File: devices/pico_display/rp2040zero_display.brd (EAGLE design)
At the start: 38.2 x 20.6 mm, 13 parts, among them U1 RP2040-ZERO'

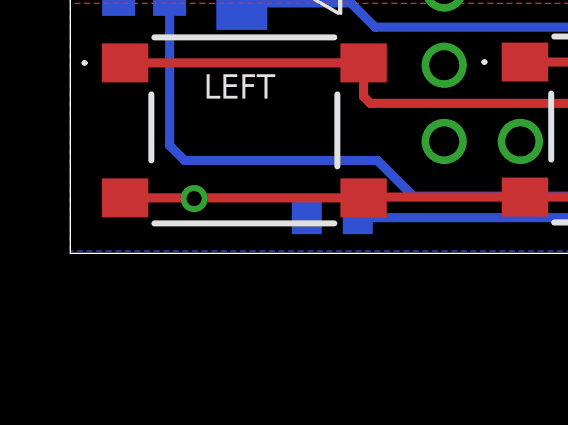
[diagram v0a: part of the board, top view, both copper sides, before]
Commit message: updates to beeper - now on main fdd board, updates to panel connectors
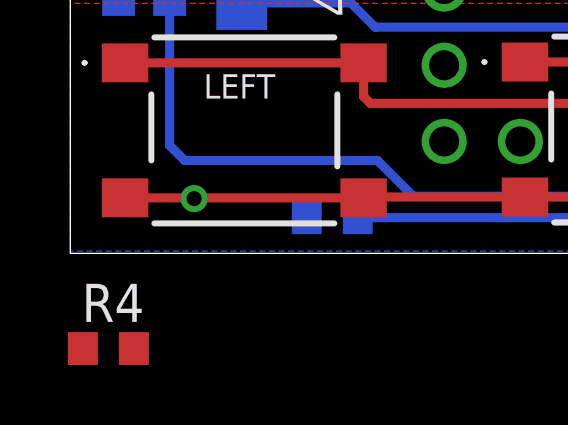
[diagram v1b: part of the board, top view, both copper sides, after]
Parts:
- added R4: 10k, resistor:R0603
- R1, R2: value 220R -> 1k
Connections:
- net RX_PANEL: now also R4.1
- net VCC: now also R4.2
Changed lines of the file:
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@@
 <attribute name="VALUE" x="10.38225" y="13.573125" size="1.27" layer="27" ratio="10" rot="R270"/>
 </element>
-<element name="R1" library="resistor" package="R0603" value="220R" x="6.429375" y="18.7325" smashed="yes" rot="MR90"/>
-<element name="R2" library="resistor" package="R0603" value="220R" x="6.429375" y="15.160625" smashed="yes" rot="MR270"/>
+<element name="R1" library="resistor" package="R0603" value="1k" x="6.429375" y="18.7325" smashed="yes" rot="MR90"/>
+<element name="R2" library="resistor" package="R0603" value="1k" x="6.429375" y="15.160625" smashed="yes" rot="MR270"/>
 <element name="D1" library="diode" package="DO214AC" value="SK110-DIO" x="5.715" y="10.398125" smashed="yes" rot="MR90"/>
 <element name="R3" library="resistor" package="R0603" value="0R" x="8.73125" y="1.190625" smashed="yes" rot="MR180"/>
@@
 <element name="R5" library="resistor" package="R0603" value="2k2" x="3.81" y="15.636875" smashed="yes" rot="MR0"/>
 <element name="R6" library="resistor" package="R0603" value="2k2" x="3.81" y="18.176875" smashed="yes" rot="MR0"/>
+<element name="R4" library="resistor" package="R0603" value="10k" x="1.27" y="-3.175"/>
 </elements>
 <signals>
@@
 <wire x1="7.166875" y1="16.010625" x2="7.699375" y2="15.478125" width="0.3048" layer="16"/>
 <wire x1="7.699375" y1="15.478125" x2="8.73125" y2="15.478125" width="0.3048" layer="16"/>
+<contactref element="R4" pad="1"/>
+<wire x1="0.42" y1="-3.175" x2="7.699375" y2="15.478125" width="0" layer="19" extent="1-16"/>
 </signal>
 <signal name="5V">
@@
 <wire x1="26.67" y1="5.08" x2="27.701875" y2="4.048125" width="0.3048" layer="16"/>
 <wire x1="27.701875" y1="4.048125" x2="27.701875" y2="3.730625" width="0.3048" layer="16"/>
+<contactref element="R4" pad="2"/>
+<wire x1="2.12" y1="-3.175" x2="3.81" y2="3.095625" width="0" layer="19" extent="1-16"/>
 </signal>
 </signals>
-<errors>
-</errors>
 </board>
 </drawing>

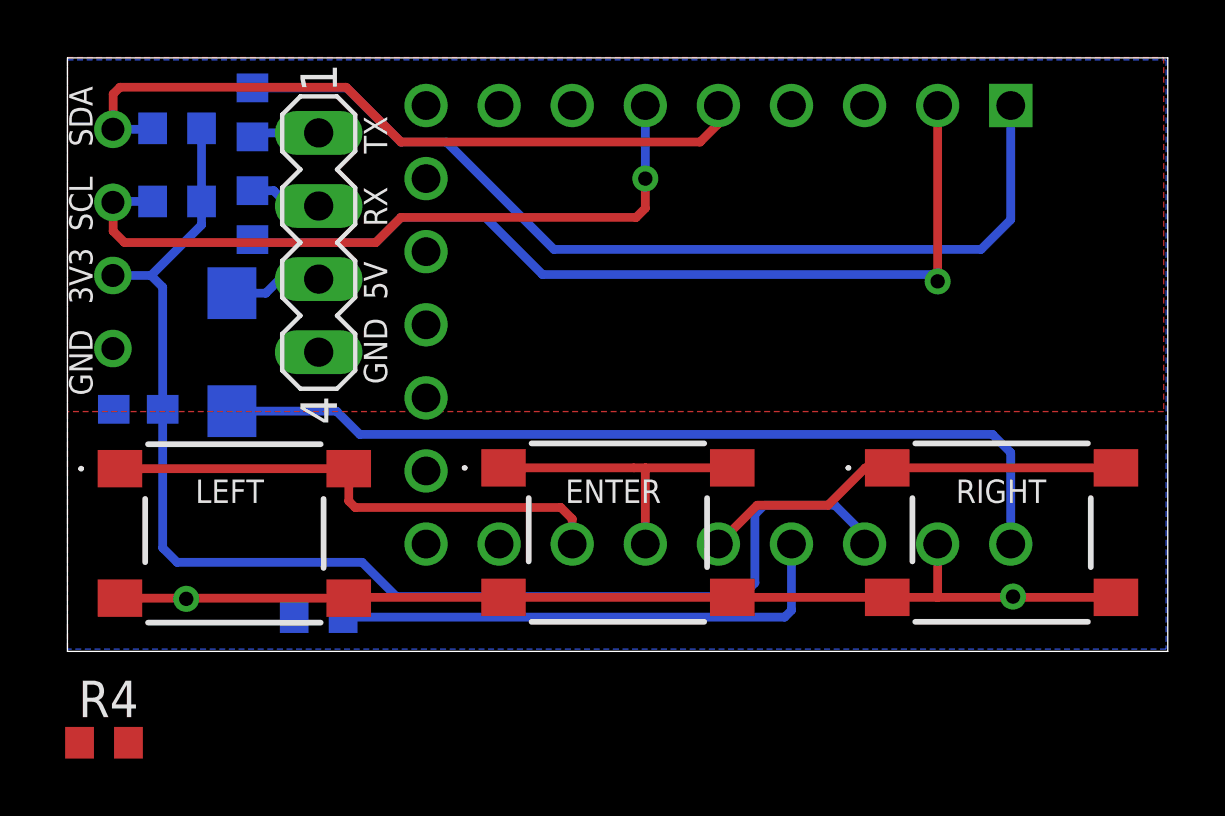
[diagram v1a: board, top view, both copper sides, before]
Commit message: routing improved on display .brd
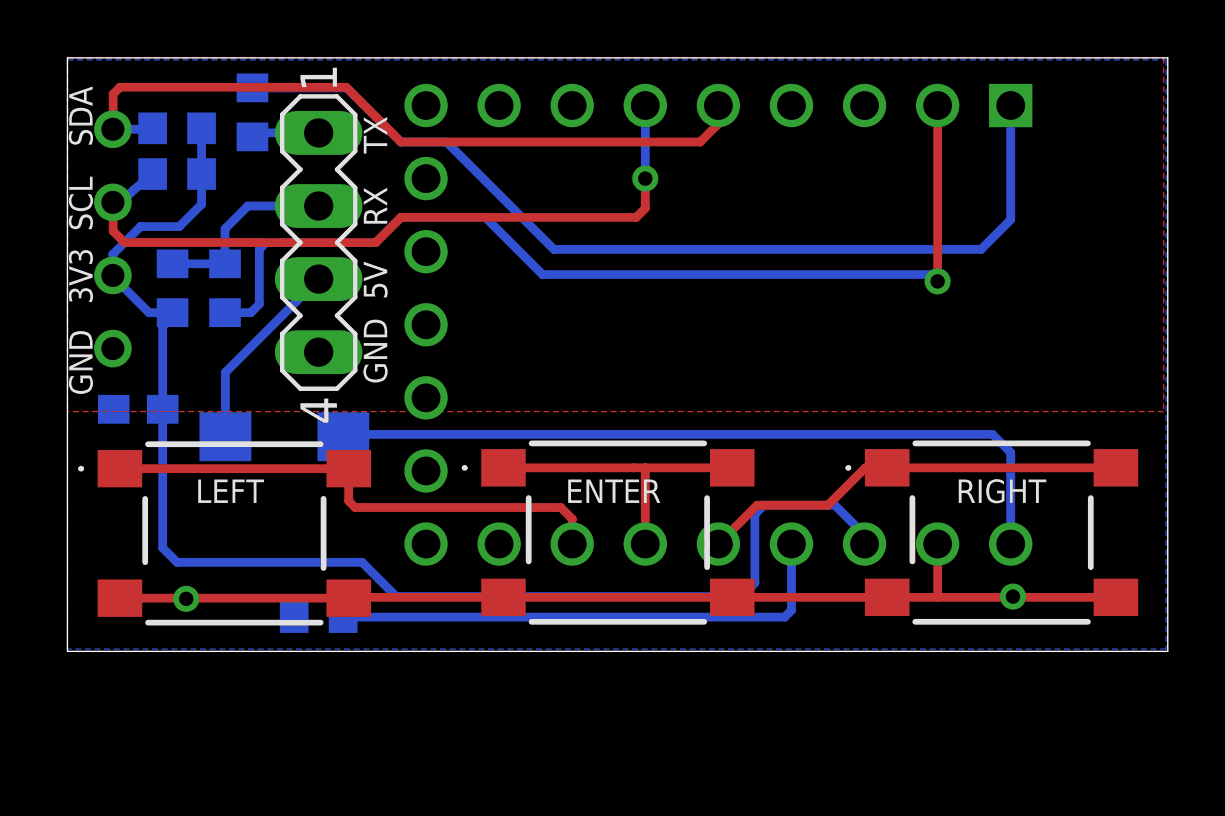
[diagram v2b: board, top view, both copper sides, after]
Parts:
- moved R4 16.0 mm to (3.65, 12.6), flipped to the bottom, turned to 270 degrees
- moved D1 3.46 mm to (7.54, 7.46), turned to 0 degrees
- moved R2 2.71 mm to (5.48, 12.6)
- moved R5 0.95 mm to (3.81, 16.6)
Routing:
- net RX_PANEL: track 2.52 -> 6.78 mm
- net N$3: track 30.8 -> 26.6 mm
- net 5V: track 3.22 -> 6.82 mm
- net N$2: track 31.3 -> 34.4 mm
- net VCC: track 45.3 -> 46.9 mm
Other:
- board text added: "CE display"
- board text added: "rev 1.0"
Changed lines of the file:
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@@
 <text x="0.873125" y="14.605" size="0.8128" layer="25" font="vector" ratio="20" rot="R90">SCL</text>
 <text x="0.873125" y="8.89" size="0.8128" layer="25" font="vector" ratio="20" rot="R90">GND</text>
-<text x="10.31875" y="9.286875" size="0.8128" layer="26" font="vector" ratio="20" rot="MR90">GND</text>
-<text x="10.239375" y="12.22375" size="0.8128" layer="26" font="vector" ratio="20" rot="MR90">5V</text>
-<text x="10.31875" y="17.30375" size="0.8128" layer="26" font="vector" ratio="20" rot="MR90">TX</text>
-<text x="10.31875" y="14.76375" size="0.8128" layer="26" font="vector" ratio="20" rot="MR90">RX</text>
+<text x="6.270625" y="9.286875" size="0.8128" layer="26" font="vector" ratio="20" rot="MR90">GND</text>
+<text x="6.270625" y="12.303125" size="0.8128" layer="26" font="vector" ratio="20" rot="MR90">5V</text>
+<text x="9.36625" y="19.05" size="0.8128" layer="26" font="vector" ratio="20" rot="MR0">TX</text>
+<text x="6.270625" y="14.9225" size="0.8128" layer="26" font="vector" ratio="20" rot="MR90">RX</text>
 <text x="11.1125" y="14.76375" size="0.8128" layer="25" font="vector" ratio="20" rot="R90">RX</text>
 <text x="11.1125" y="17.30375" size="0.8128" layer="25" font="vector" ratio="20" rot="R90">TX</text>
@@
 <text x="30.876875" y="5.159375" size="0.8128" layer="25" font="vector" ratio="20">RIGHT</text>
 <text x="17.30375" y="5.159375" size="0.8128" layer="25" font="vector" ratio="20">ENTER</text>
+<rectangle x1="6.588125" y1="6.588125" x2="8.41375" y2="8.334375" layer="42"/>
+<text x="9.8425" y="4.60375" size="1.016" layer="26" font="vector" ratio="20" rot="MR0">CE display</text>
+<text x="9.8425" y="3.175" size="1.016" layer="26" font="vector" ratio="20" rot="MR0">rev 1.0</text>
 </plain>
 <attributes>
@@
 </element>
 <element name="R1" library="resistor" package="R0603" value="1k" x="6.429375" y="18.7325" smashed="yes" rot="MR90"/>
-<element name="R2" library="resistor" package="R0603" value="1k" x="6.429375" y="15.160625" smashed="yes" rot="MR270"/>
-<element name="D1" library="diode" package="DO214AC" value="SK110-DIO" x="5.715" y="10.398125" smashed="yes" rot="MR90"/>
+<element name="R2" library="resistor" package="R0603" value="1k" x="5.476875" y="12.620625" smashed="yes" rot="MR270"/>
+<element name="D1" library="diode" package="DO214AC" value="SK110-DIO" x="7.540625" y="7.46125" smashed="yes" rot="MR0"/>
 <element name="R3" library="resistor" package="R0603" value="0R" x="8.73125" y="1.190625" smashed="yes" rot="MR180"/>
 <element name="S1" library="DTSM-62N-V-B" package="DTSM62NVB" value="DTSM-62N-V-B" x="5.800625" y="4.099375" smashed="yes">
@@
 <attribute name="VALUE" x="3.095625" y="6.50875" size="1.27" layer="28" rot="MR0"/>
 </element>
-<element name="R5" library="resistor" package="R0603" value="2k2" x="3.81" y="15.636875" smashed="yes" rot="MR0"/>
+<element name="R5" library="resistor" package="R0603" value="2k2" x="3.81" y="16.589375" smashed="yes" rot="MR0"/>
 <element name="R6" library="resistor" package="R0603" value="2k2" x="3.81" y="18.176875" smashed="yes" rot="MR0"/>
-<element name="R4" library="resistor" package="R0603" value="10k" x="1.27" y="-3.175"/>
+<element name="R4" library="resistor" package="R0603" value="10k" x="3.65125" y="12.620625" smashed="yes" rot="MR270"/>
 </elements>
 <signals>
@@
 <contactref element="SV1" pad="2"/>
 <contactref element="R2" pad="1"/>
-<wire x1="6.429375" y1="16.010625" x2="7.166875" y2="16.010625" width="0.3048" layer="16"/>
-<wire x1="7.166875" y1="16.010625" x2="7.699375" y2="15.478125" width="0.3048" layer="16"/>
-<wire x1="7.699375" y1="15.478125" x2="8.73125" y2="15.478125" width="0.3048" layer="16"/>
 <contactref element="R4" pad="1"/>
-<wire x1="0.42" y1="-3.175" x2="7.699375" y2="15.478125" width="0" layer="19" extent="1-16"/>
+<wire x1="3.65125" y1="13.470625" x2="3.81" y2="13.6525" width="0.3048" layer="16"/>
+<wire x1="3.81" y1="13.6525" x2="3.991875" y2="13.470625" width="0.3048" layer="16"/>
+<wire x1="3.991875" y1="13.470625" x2="5.476875" y2="13.470625" width="0.3048" layer="16"/>
+<wire x1="5.476875" y1="13.470625" x2="5.476875" y2="14.684375" width="0.3048" layer="16"/>
+<wire x1="5.476875" y1="14.684375" x2="6.270625" y2="15.478125" width="0.3048" layer="16"/>
+<wire x1="6.270625" y1="15.478125" x2="8.73125" y2="15.478125" width="0.3048" layer="16"/>
 </signal>
 <signal name="5V">
 <contactref element="SV1" pad="3"/>
 <contactref element="D1" pad="A"/>
-<wire x1="5.715" y1="12.448125" x2="6.891875" y2="12.448125" width="0.3048" layer="16"/>
-<wire x1="6.891875" y1="12.448125" x2="7.381875" y2="12.938125" width="0.3048" layer="16"/>
-<wire x1="7.381875" y1="12.938125" x2="8.73125" y2="12.938125" width="0.3048" layer="16"/>
+<wire x1="5.490625" y1="7.46125" x2="5.490625" y2="9.6975" width="0.3048" layer="16"/>
+<wire x1="5.490625" y1="9.6975" x2="8.73125" y2="12.938125" width="0.3048" layer="16"/>
 </signal>
 <signal name="N$1">
@@
 <contactref element="U1" pad="2"/>
 <contactref element="R2" pad="2"/>
-<wire x1="6.429375" y1="14.310625" x2="6.531875" y2="14.208125" width="0.3048" layer="16"/>
-<wire x1="6.531875" y1="14.208125" x2="10.715625" y2="14.208125" width="0.3048" layer="16"/>
 <wire x1="10.715625" y1="14.208125" x2="11.58875" y2="15.08125" width="0.3048" layer="16"/>
 <wire x1="11.58875" y1="15.08125" x2="14.525625" y2="15.08125" width="0.3048" layer="16"/>
@@
 <via x="30.241875" y="12.85875" extent="1-16" drill="0.5"/>
 <wire x1="30.241875" y1="12.85875" x2="30.241875" y2="18.970625" width="0.3048" layer="1"/>
+<wire x1="5.476875" y1="11.770625" x2="6.373125" y2="11.770625" width="0.3048" layer="16"/>
+<wire x1="6.373125" y1="11.770625" x2="6.6675" y2="12.065" width="0.3048" layer="16"/>
+<wire x1="6.6675" y1="12.065" x2="6.6675" y2="13.97" width="0.3048" layer="16"/>
+<wire x1="6.6675" y1="13.97" x2="6.905625" y2="14.208125" width="0.3048" layer="16"/>
+<wire x1="6.905625" y1="14.208125" x2="10.715625" y2="14.208125" width="0.3048" layer="16"/>
 </signal>
 <signal name="GND">
@@
 <contactref element="R5" pad="2"/>
 <wire x1="1.579375" y1="15.604375" x2="1.579375" y2="15.636875" width="0.3048" layer="16"/>
-<wire x1="1.579375" y1="15.636875" x2="2.96" y2="15.636875" width="0.3048" layer="16"/>
 <wire x1="20.081875" y1="18.970625" x2="20.081875" y2="16.430625" width="0.3048" layer="16"/>
 <via x="20.081875" y="16.430625" extent="1-16" drill="0.5"/>
@@
 <wire x1="1.5875" y1="14.605" x2="1.5875" y2="15.59625" width="0.3048" layer="1"/>
 <wire x1="1.5875" y1="15.59625" x2="1.579375" y2="15.604375" width="0.3048" layer="1"/>
+<wire x1="2.96" y1="16.589375" x2="2.301875" y2="16.03375" width="0.3048" layer="16"/>
+<wire x1="2.301875" y1="16.03375" x2="1.896875" y2="15.62875" width="0.3048" layer="16"/>
+<wire x1="1.896875" y1="15.62875" x2="1.579375" y2="15.604375" width="0.3048" layer="16"/>
 </signal>
 <signal name="BTN_LEFT_ENC_A">
@@
 <contactref element="D1" pad="C"/>
 <contactref element="U1" pad="23"/>
-<wire x1="5.715" y1="8.348125" x2="9.3525" y2="8.348125" width="0.3048" layer="16"/>
-<wire x1="9.3525" y1="8.348125" x2="10.16" y2="7.540625" width="0.3048" layer="16"/>
+<wire x1="9.590625" y1="7.46125" x2="9.908125" y2="7.554375" width="0.3048" layer="16"/>
+<wire x1="9.908125" y1="7.554375" x2="10.16" y2="7.540625" width="0.3048" layer="16"/>
 <wire x1="10.16" y1="7.540625" x2="32.146875" y2="7.540625" width="0.3048" layer="16"/>
 <wire x1="32.146875" y1="7.540625" x2="32.781875" y2="6.905625" width="0.3048" layer="16"/>
@@
 <contactref element="R5" pad="1"/>
 <contactref element="U1" pad="21"/>
-<wire x1="4.66" y1="15.636875" x2="4.66" y2="18.176875" width="0.3048" layer="16"/>
-<wire x1="1.579375" y1="13.064375" x2="2.904375" y2="13.064375" width="0.3048" layer="16"/>
-<wire x1="2.904375" y1="13.064375" x2="4.66" y2="14.82" width="0.3048" layer="16"/>
-<wire x1="4.66" y1="14.82" x2="4.66" y2="15.636875" width="0.3048" layer="16"/>
-<wire x1="3.310625" y1="8.41375" x2="3.310625" y2="12.658125" width="0.3048" layer="16"/>
-<wire x1="3.310625" y1="12.658125" x2="2.904375" y2="13.064375" width="0.3048" layer="16"/>
+<wire x1="4.66" y1="16.589375" x2="4.66" y2="18.176875" width="0.3048" layer="16"/>
 <wire x1="3.310625" y1="8.41375" x2="3.310625" y2="3.595" width="0.3048" layer="16"/>
 <wire x1="3.310625" y1="3.595" x2="3.81" y2="3.095625" width="0.3048" layer="16"/>
@@
 <wire x1="27.701875" y1="4.048125" x2="27.701875" y2="3.730625" width="0.3048" layer="16"/>
 <contactref element="R4" pad="2"/>
-<wire x1="2.12" y1="-3.175" x2="3.81" y2="3.095625" width="0" layer="19" extent="1-16"/>
+<wire x1="3.310625" y1="8.41375" x2="3.310625" y2="11.27125" width="0.3048" layer="16"/>
+<wire x1="3.310625" y1="11.27125" x2="3.65125" y2="11.770625" width="0.3048" layer="16"/>
+<wire x1="4.66" y1="16.328125" x2="4.66" y2="16.589375" width="0.3048" layer="16"/>
+<wire x1="3.65125" y1="11.770625" x2="2.834375" y2="11.770625" width="0.3048" layer="16"/>
+<wire x1="2.834375" y1="11.770625" x2="1.579375" y2="13.025625" width="0.3048" layer="16"/>
+<wire x1="1.579375" y1="13.025625" x2="1.579375" y2="13.064375" width="0.3048" layer="16"/>
+<wire x1="1.579375" y1="13.064375" x2="1.579375" y2="13.803125" width="0.3048" layer="16"/>
+<wire x1="1.579375" y1="13.803125" x2="2.54" y2="14.76375" width="0.3048" layer="16"/>
+<wire x1="2.54" y1="14.76375" x2="3.889375" y2="14.76375" width="0.3048" layer="16"/>
+<wire x1="3.889375" y1="14.76375" x2="4.66" y2="15.534375" width="0.3048" layer="16"/>
+<wire x1="4.66" y1="15.534375" x2="4.66" y2="16.589375" width="0.3048" layer="16"/>
 </signal>
 </signals>
